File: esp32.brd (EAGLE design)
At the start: 91.4 x 100 mm, 49 parts, among them IC1 PEC11R-4230K-S0024, IC2 AD8532ARZ, T1 BST82-1, T2 BST82-1, U1 ESP32-WROOM-32D, X1 JST-XH-02-PIN-LONG-PAD, X2 JST-XH-03-PIN-LONG-PAD, X3 JST-XH-03-PIN-LONG-PAD, X4 JST-XH-02-PIN-LONG-PAD

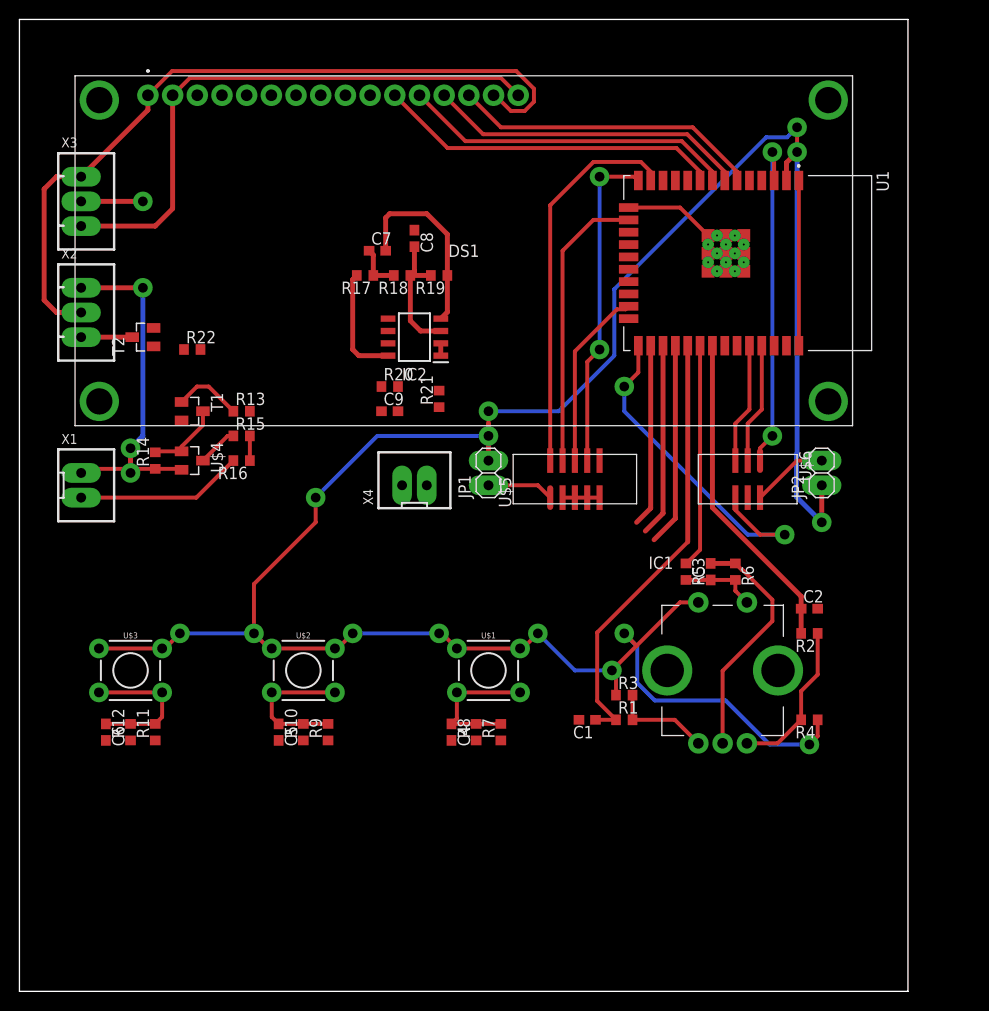
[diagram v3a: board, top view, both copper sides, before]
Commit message: La till hål i ytterkanterna.
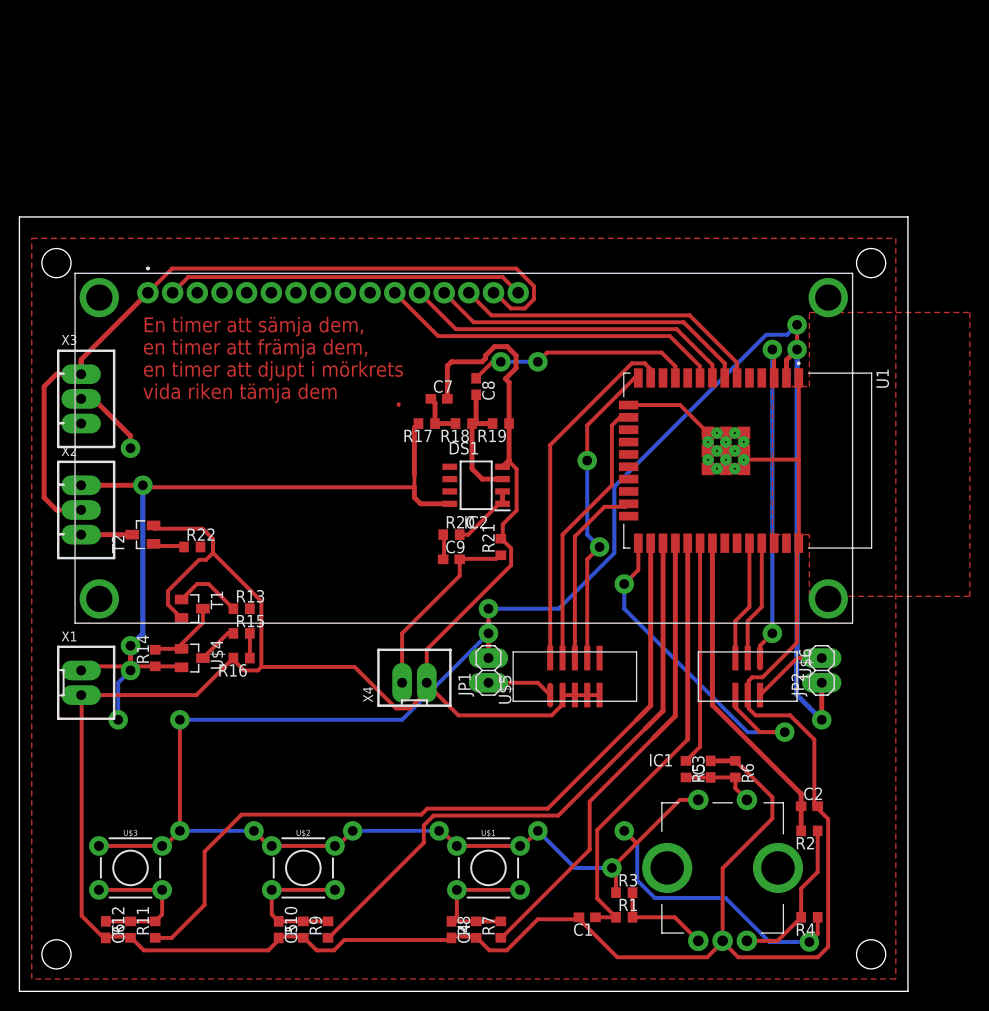
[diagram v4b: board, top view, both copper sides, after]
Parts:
- moved R22 20.3 mm to (17.8, 45.7)
- moved U1 20.3 mm to (74.9, 54.6)
- moved IC1 20.3 mm to (69.8, 12.7)
- moved U$1 20.3 mm to (48.3, 12.7)
- moved U$2 20.3 mm to (29.2, 12.7)
- moved U$3 20.3 mm to (11.4, 12.7)
- moved C1 20.3 mm to (58.4, 7.62)
- moved C3 20.3 mm to (71.1, 22.9)
- moved C4 20.3 mm to (44.5, 6.35)
- moved C5 20.3 mm to (26.7, 6.35)
- moved C6 20.3 mm to (8.89, 6.35)
- moved DS1 20.3 mm to (45.7, 55.9)
- moved JP1 20.3 mm to (48.3, 33.0)
- moved JP2 20.3 mm to (82.5, 33.0)
- moved R1 20.3 mm to (62.2, 7.62)
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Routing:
- net GND: track 150.8 -> 419.7 mm
- net BTN_3: track 18.8 -> 80.8 mm
- net BTN_2: track 19.8 -> 62.4 mm
- net VCC: track 50.3 -> 83.9 mm, vias 3 -> 4
- net BTN_1: track 20.9 -> 48.1 mm
- net AUDIO_FROM_ESP32: track 0.00 -> 23.4 mm, vias 0 -> 2
- net SPEAKER_OUT: track 0.00 -> 19.5 mm
- net +3V3: track 242.9 -> 252.7 mm
- net N$12: track 1.27 -> 7.00 mm
- net N$11: track 0.00 -> 3.31 mm
- net TMS: track 39.8 -> 36.9 mm
- net N$14: track 0.00 -> 2.68 mm
- net +5V: track 79.4 -> 81.9 mm
- net TDI: track 33.9 -> 32.3 mm
- net TCK: track 29.7 -> 28.1 mm
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- added copper zone on layer 1, net GND
- added copper zone on layer 1, net N$16
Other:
- board size 91.4 x 100 mm -> 91.4 x 79.7 mm
- board text added: "En timer att sämja dem, en timer att främja dem, en timer att djupt i mörkrets vida riken tämja dem"

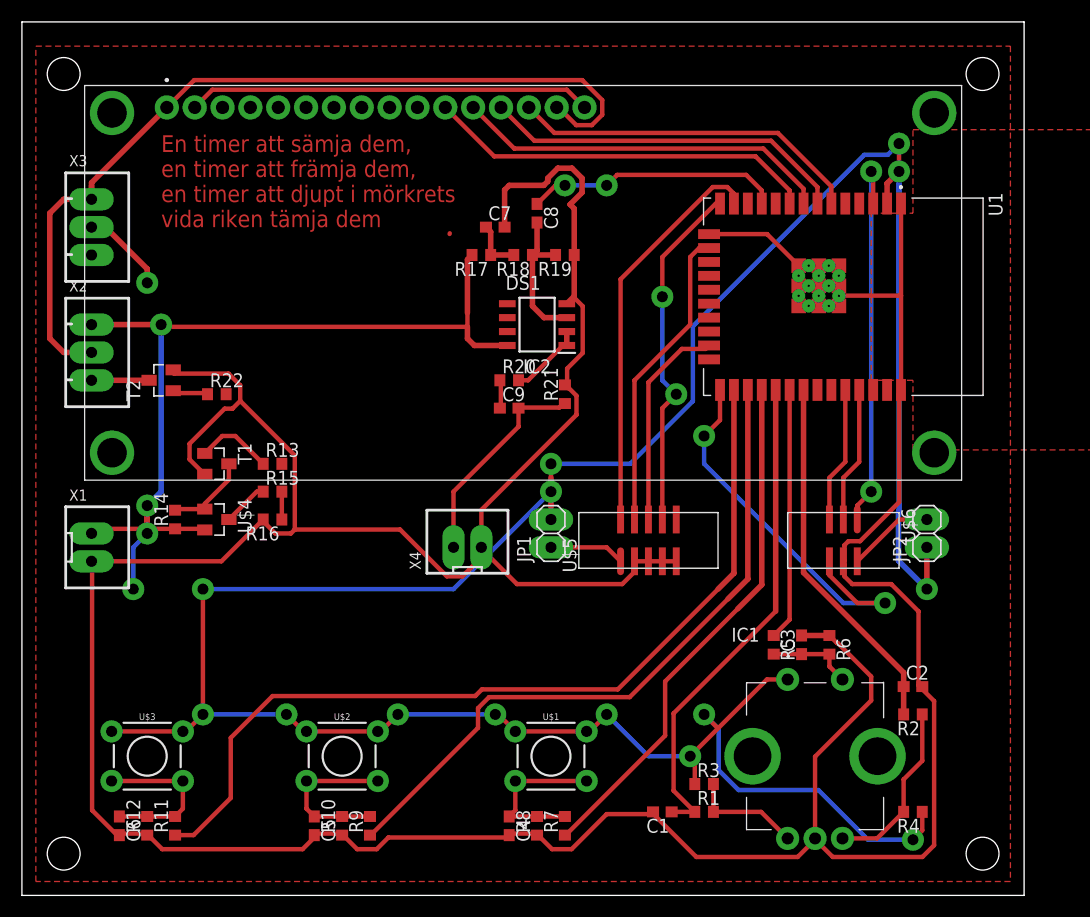
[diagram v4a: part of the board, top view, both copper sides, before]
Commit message: Kom på att man ska lägga till en reset-knapp... Men saknar fortfarande massa kondingar och sen 3.3V regulator.
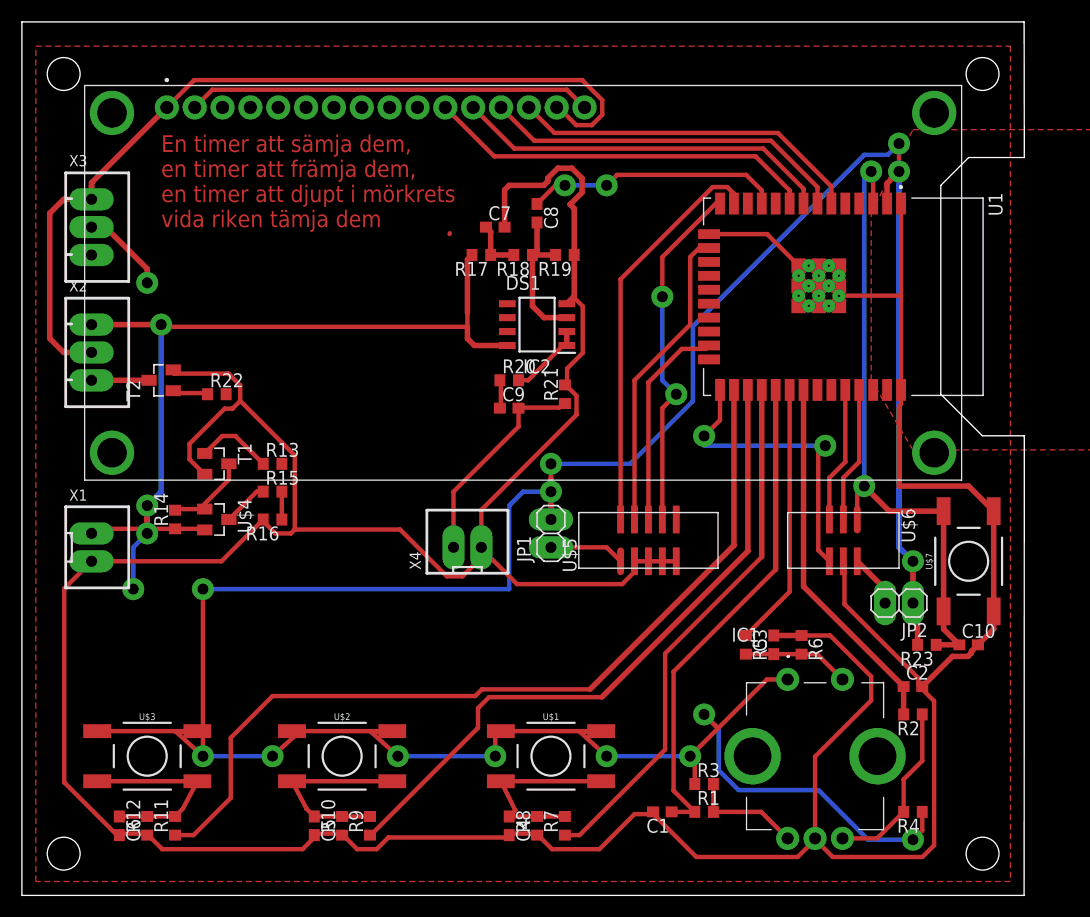
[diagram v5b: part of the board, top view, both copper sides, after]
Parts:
- added C10: 0.1uF, rcl:C0603
- added R23: 10K, rcl:R0603
- added U$7: PUSH_BUTTONSMD, Test:TACTILE_SWITCH_PTH_6.0MM_SMD
- IC1: value PEC11R-4230K-S0024 -> PEC11R-4230K-S00243D
- U$1, U$2, U$3: value PUSH_BUTTON -> PUSH_BUTTONSMD; device Test:TACTILE_SWITCH_PTH_6.0MM -> Test:TACTILE_SWITCH_PTH_6.0MM_SMD
- moved JP2 6.84 mm to (80.0, 26.7), turned to 180 degrees
- moved C3 2.54 mm to (68.6, 22.9)
- moved R5 2.54 mm to (66.0, 22.9)
- moved R6 2.54 mm to (71.1, 22.9)
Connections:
- net +3V3: now also R23.2, U$1.P$1, U$1.P$2, U$2.P$1, U$2.P$2, U$3.P$1, U$3.P$2; no longer U$1.1, U$1.2, U$2.1, U$2.2, U$3.1, U$3.2
- net ESP_EN: now also C10.1, R23.1, U$7.P$1, U$7.P$2
- net GND: now also C10.2, U$7.P$3, U$7.P$4
- net N$3: now also U$1.P$3, U$1.P$4; no longer U$1.3, U$1.4
- net N$6: now also U$2.P$3, U$2.P$4; no longer U$2.3, U$2.4
- net N$8: now also U$3.P$3, U$3.P$4; no longer U$3.3, U$3.4
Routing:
- net +3V3: track 252.7 -> 277.1 mm
- net ESP_EN: track 35.3 -> 58.8 mm
- net GND: track 419.7 -> 442.5 mm
- net ESP_IO_0: track 36.5 -> 28.0 mm
- net N$22: track 7.93 -> 4.86 mm
- net N$8: track 15.1 -> 18.1 mm
- net N$6: track 15.1 -> 18.1 mm
- net N$3: track 15.1 -> 18.0 mm
- net N$9: track 7.88 -> 9.77 mm
- net BTN_3: track 80.8 -> 79.3 mm
- net BTN_2: track 62.4 -> 61.0 mm
- net ROT_ENC_BTN: track 23.0 -> 24.1 mm
- net BTN_1: track 48.1 -> 48.8 mm
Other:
- outline, holes or cut-outs redrawn

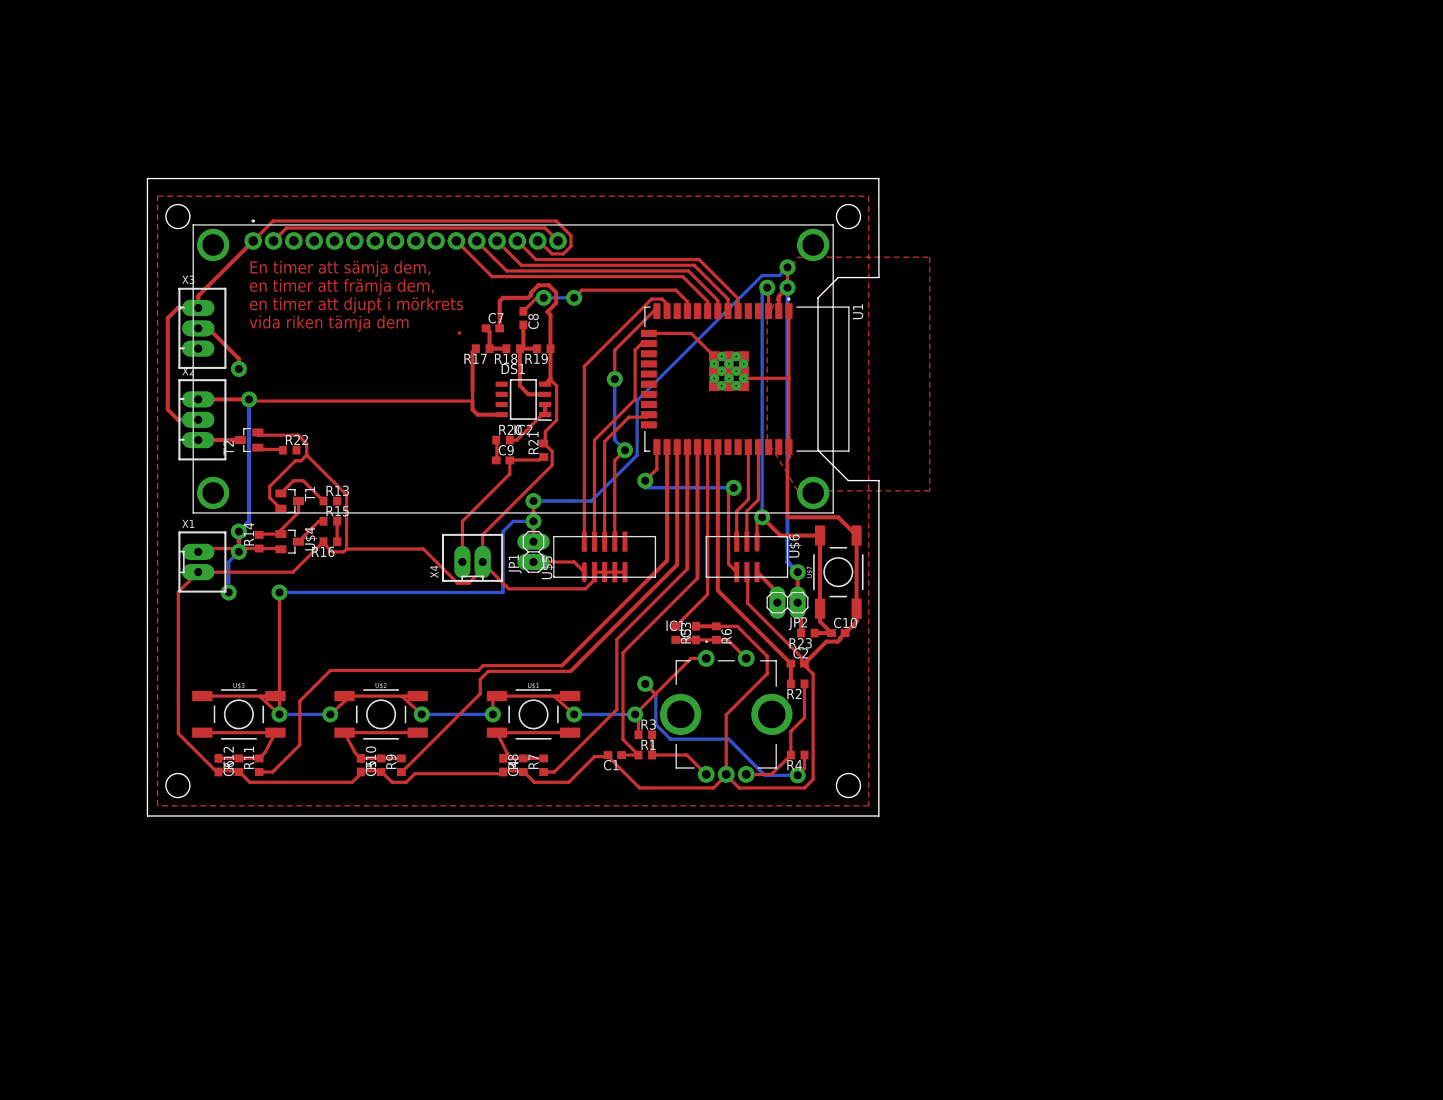
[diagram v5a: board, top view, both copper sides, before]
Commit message: La till kondingar och kopplade alla signaler, precis lagom många GPIO pinnar på ESP32an typ bara 2 över!
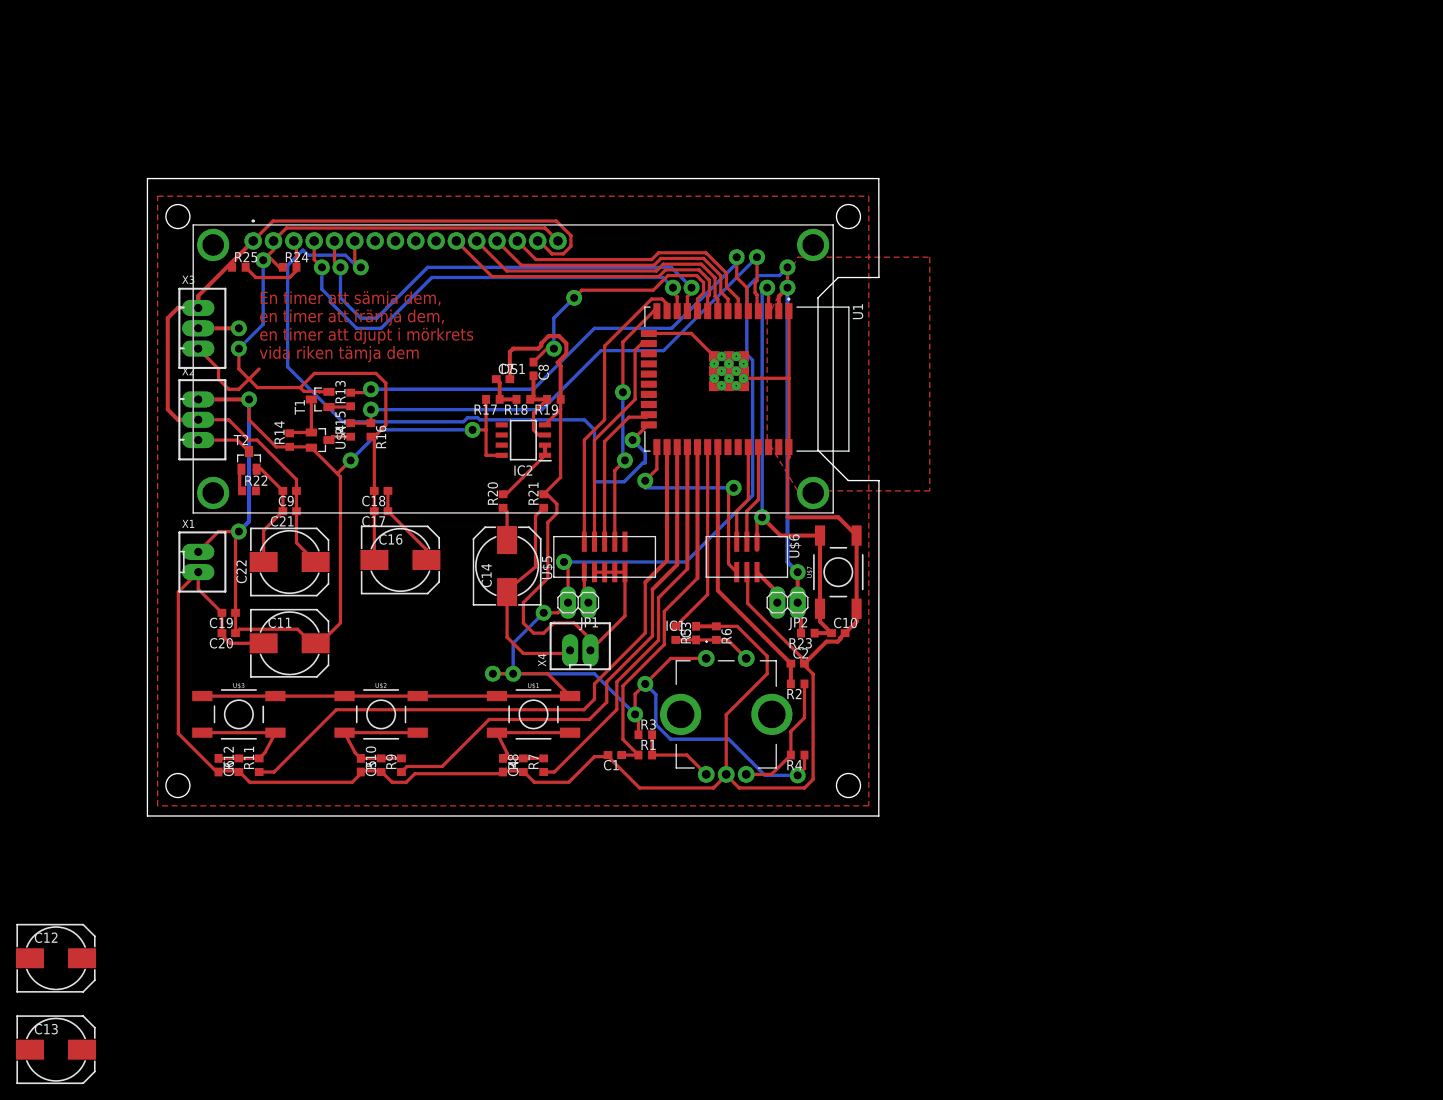
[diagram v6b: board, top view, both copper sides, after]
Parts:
- added C11, C12, C13, C16, C22: (no value), rcl:140CLH-0810
- added C14: 270uF, rcl:140CLH-0810
- added C17, C18, C19, C20: 0.1uF, rcl:C0603
- added C21: 10uF, rcl:C0603
- added R24, R25: 100, rcl:R0603
- C9: value 270uF -> 10uF
- moved C9 26.9 mm to (17.8, 40.6), turned to 180 degrees
- moved X4 17.4 mm to (54.1, 20.7)
- moved R16 14.9 mm to (27.9, 48.3), turned to 270 degrees
- moved R14 13.3 mm to (17.8, 47.0)
- moved T1 13.3 mm to (21.6, 52.1), turned to 90 degrees
- moved U$4 13.3 mm to (21.6, 47.0)
- moved R13 13.0 mm to (25.4, 52.1), turned to 90 degrees
- moved R15 11.7 mm to (25.4, 48.3), turned to 90 degrees
- moved JP1 8.46 mm to (53.8, 26.7), turned to 180 degrees
- moved R20 7.62 mm to (44.5, 39.4), turned to 90 degrees
- moved R22 7.18 mm to (12.7, 40.6)
- moved C7 6.48 mm to (44.5, 54.6)
- moved R17 6.48 mm to (43.2, 52.1)
- moved R18 6.48 mm to (47.0, 52.1)
- moved R19 6.48 mm to (50.8, 52.1)
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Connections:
- removed net N$20: DS1.4
- new net LCD_RS: DS1.4, U1.12
- new net N$17: DS1.3, R24.2, R25.2
- net +3V3: now also C16.+, C17.1, C18.1
- net +5V: now also C21.1, C22.+, C9.1, R25.1
- net AUDIO_FROM_ESP32: now also U1.10; no longer U1.11
- net BAT_MONITOR_ANALOG: now also U1.4
- net BAT_MONITOR_ENABLE: now also U1.5
- net GND: now also C11.-, C16.-, C17.2, C18.2, C19.2, C20.2, C21.2, C22.-, C9.2, R24.1
- net LCD_E: now also U1.24
- net LCD_RW: now also U1.11
- net N$14: now also C14.+; no longer C9.1
- net SPEAKER_OUT: now also C14.-; no longer C9.2
- net VCC: now also C11.+, C19.1, C20.1
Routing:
- net LCD_E: track 0.00 -> 89.3 mm, vias 0 -> 2
- net BAT_MONITOR_ANALOG: track 2.54 -> 67.4 mm, vias 0 -> 2
- net BAT_MONITOR_ENABLE: track 0.00 -> 63.1 mm, vias 0 -> 2
- net LCD_RW: track 0.00 -> 59.2 mm, vias 0 -> 2
- net LCD_RS: track 0.00 -> 59.0 mm, vias 0 -> 2
- net GND: track 442.5 -> 487.4 mm, vias 0 -> 2
- net VCC: track 83.9 -> 123.6 mm
- net +5V: track 81.9 -> 109.2 mm
- net +3V3: track 277.1 -> 259.8 mm, vias 14 -> 10
- net N$17: track 0.00 -> 11.1 mm
- net AUDIO_FROM_ESP32: track 23.4 -> 32.2 mm
- net SPEAKER_OUT: track 19.5 -> 27.3 mm
- net N$13: track 7.04 -> 2.75 mm
- net BTN_2: track 61.0 -> 64.8 mm
- net N$24: track 6.88 -> 4.02 mm
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
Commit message: Fixade så att texten har orphans i fyllkomandot, såg konstigt ut annars.
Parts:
- removed C12, C13: (no value), rcl:140CLH-0810
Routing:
- removed copper zone on layer 1, net N$16

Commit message: Added dimmer for lcd and starting redouting to 18mil
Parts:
- added R26: 100, rcl:R0603
- added T3: BST82-1, Test:SOT23
- moved R21 1.80 mm to (48.3, 40.6)
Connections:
- new net LCD_DIMMER: R26.2
- new net N$16: R26.1, T3.1
- new net N$18: DS1.16, T3.3
- net GND: now also T3.2; no longer DS1.16
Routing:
- net LCD_D4: track 38.3 -> 0.00 mm
- net TMS: track 36.9 -> 0.00 mm
- net LCD_D5: track 36.7 -> 0.00 mm
- net LCD_D6: track 35.3 -> 0.00 mm
- net LCD_D7: track 33.9 -> 0.00 mm
- net +3V3: track 259.8 -> 287.3 mm
- net AUDIO_FROM_ESP32: track 32.2 -> 8.85 mm
- net +5V: track 109.2 -> 125.8 mm, vias 0 -> 2
- net LCD_RW: track 59.2 -> 46.3 mm
- net LCD_E: track 89.3 -> 77.3 mm
- net LCD_RS: track 59.0 -> 47.4 mm
- net TDI: track 31.4 -> 20.4 mm
- net BAT_MONITOR_ENABLE: track 63.1 -> 55.7 mm
- net BAT_MONITOR_ANALOG: track 67.4 -> 60.4 mm
- net ESP_EN: track 58.8 -> 55.8 mm
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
